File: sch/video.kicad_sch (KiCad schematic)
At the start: 16 parts

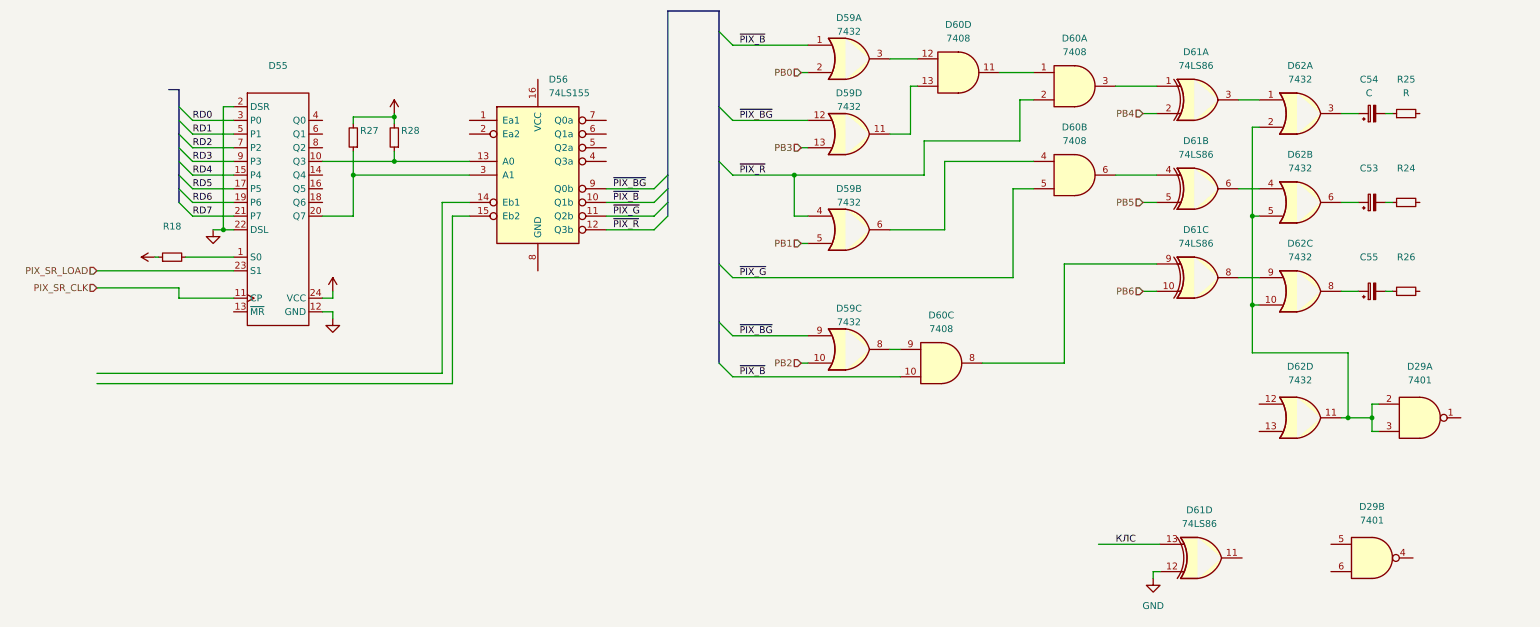
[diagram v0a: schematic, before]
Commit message: Video part schematic almost complete
No output connector added, also it needs some review / reality check.
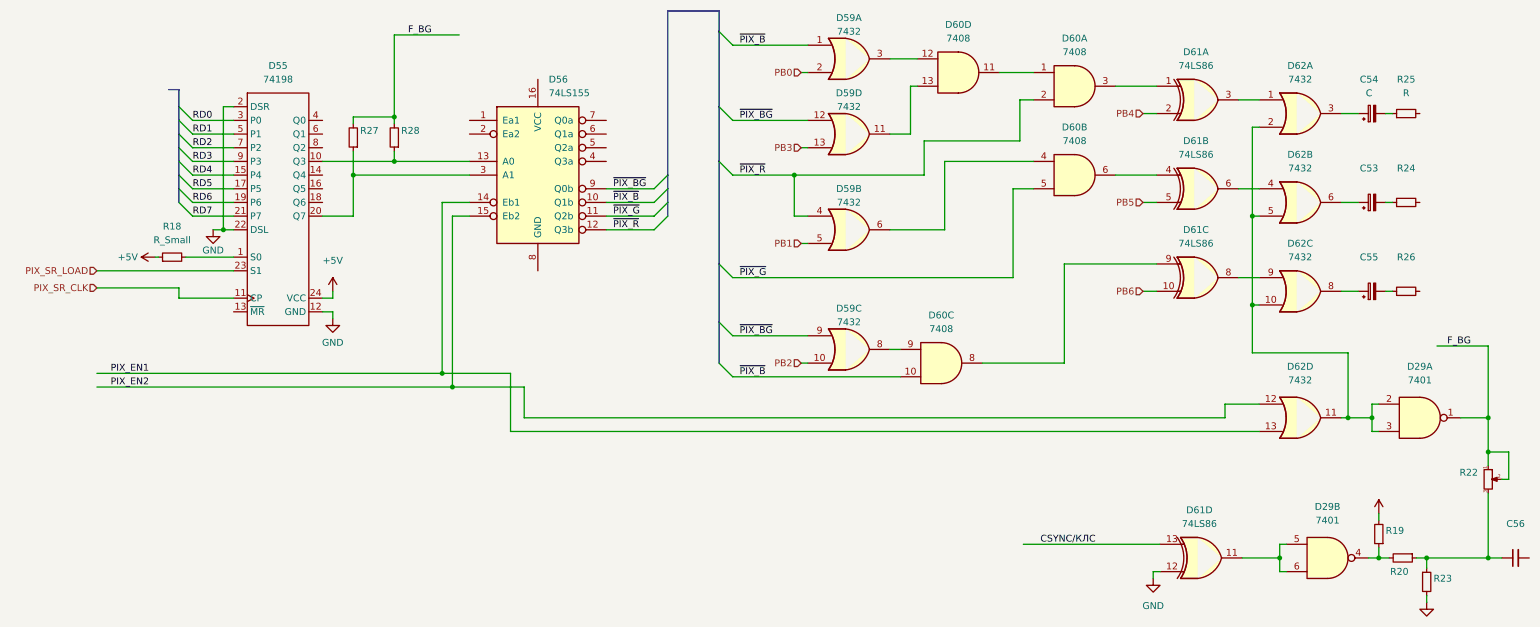
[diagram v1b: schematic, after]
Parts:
- added C56: (no value), symbol Device:C_Small
- added R19, R20, R23: ~, symbol Device:R_Small
- added R22: (no value), symbol Device:R_Potentiometer_Small
- D55: value (none) -> 74198
- R18: value (none) -> R_Small
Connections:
- net +5V: now also R19.2; no longer R27.2, R28.2
- net GND: now also R23.2
- net PIX_EN1: now reaches D56.14 (Eb1)
- net PIX_EN1: now also D62.13
- net PIX_EN2: now reaches D56.15 (Eb2)
- net PIX_EN2: now also D62.12
- net at D61.11: now also D29.5, D29.6
- net at D29.4: now also R19.1, R20.2
- net F_BG: now reaches D29.1
- net F_BG: now also R27.2, R28.2, R22.1, R22.2
- net КЛС renamed CSYNC/КЛС
- new net: C56.1, R20.1, R22.3, R23.1
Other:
- moved on the sheet: D29B

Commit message: Sch: added PIO sheet
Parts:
- C56: value (none) -> C_Small
- R22: value (none) -> !
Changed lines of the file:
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@@
       (effects (font (size 1.27 1.27)) hide)
     )
-    (property "Value" "" (id 1) (at 344.805 125.095 0))
+    (property "Value" "+5V" (id 1) (at 344.805 125.095 0))
     (property "Footprint" "" (id 2) (at 344.805 128.905 0)
       (effects (font (size 1.27 1.27)) hide)
@@
       (effects (font (size 1.27 1.27)) (justify right))
     )
-    (property "Value" "" (id 1) (at 363.22 123.8249 0)
+    (property "Value" "!" (id 1) (at 363.22 123.8249 0)
       (effects (font (size 1.27 1.27)) (justify right))
     )
@@
     (in_bom yes) (on_board yes) (fields_autoplaced)
     (property "Reference" "C56" (id 0) (at 370.2113 130.81 90))
-    (property "Value" "" (id 1) (at 370.2113 133.35 90))
+    (property "Value" "C_Small" (id 1) (at 370.2113 133.35 90))
     (property "Footprint" "" (id 2) (at 370.205 137.16 0)
       (effects (font (size 1.27 1.27)) hide)
@@
       (effects (font (size 1.27 1.27)) hide)
     )
-    (property "Value" "" (id 1) (at 353.695 149.86 0))
+    (property "Value" "GND" (id 1) (at 353.695 149.86 0))
     (property "Footprint" "" (id 2) (at 353.695 145.415 0)
       (effects (font (size 1.27 1.27)) hide)

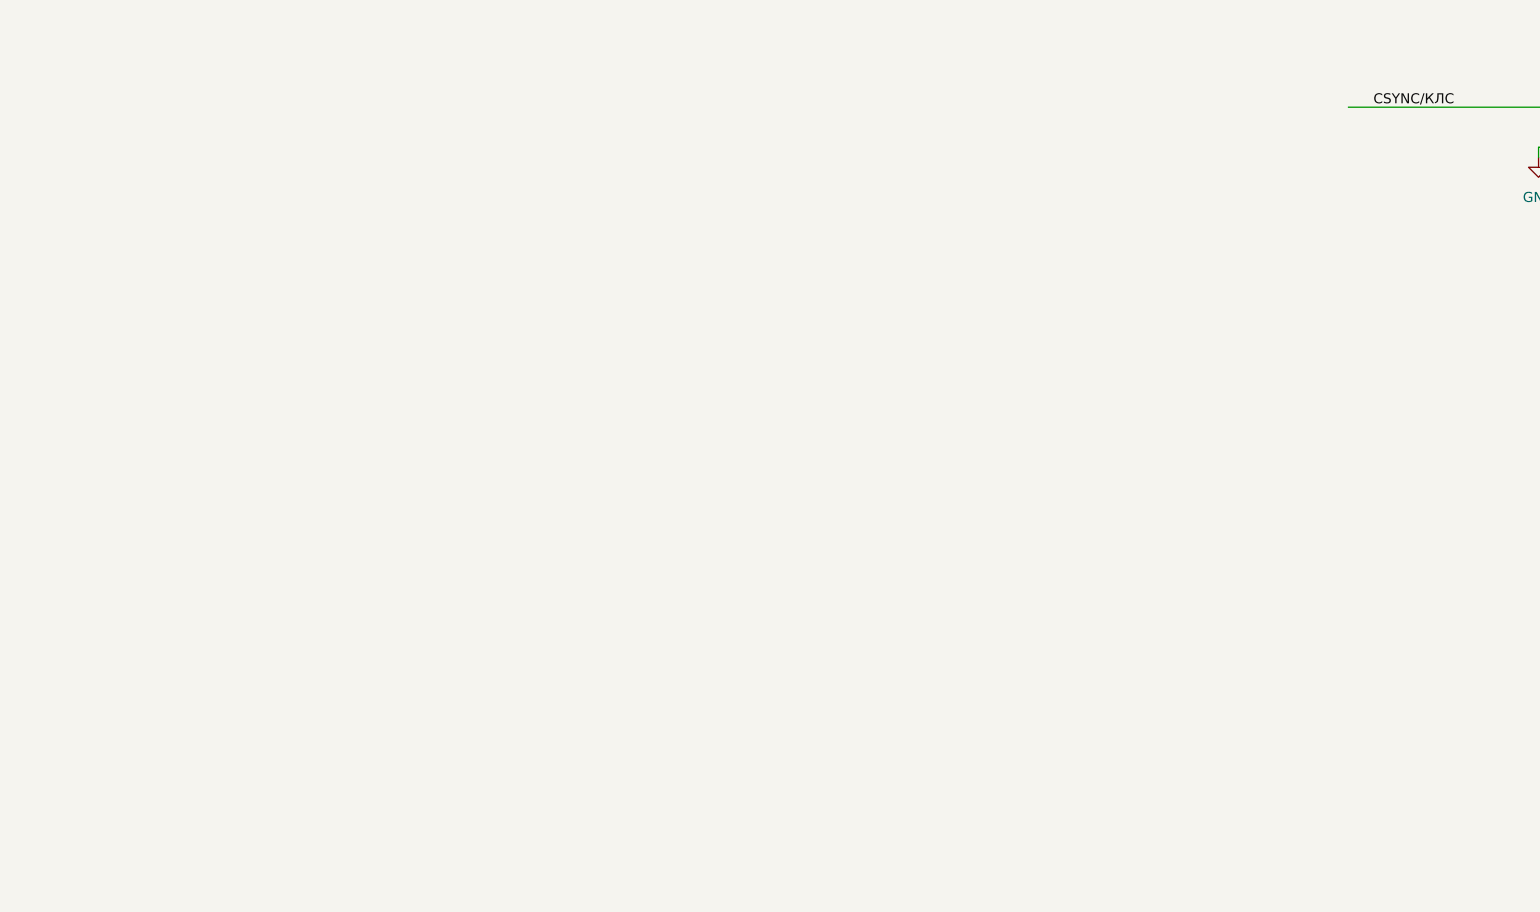
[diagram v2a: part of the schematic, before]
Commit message: Sch: timing counters block completed
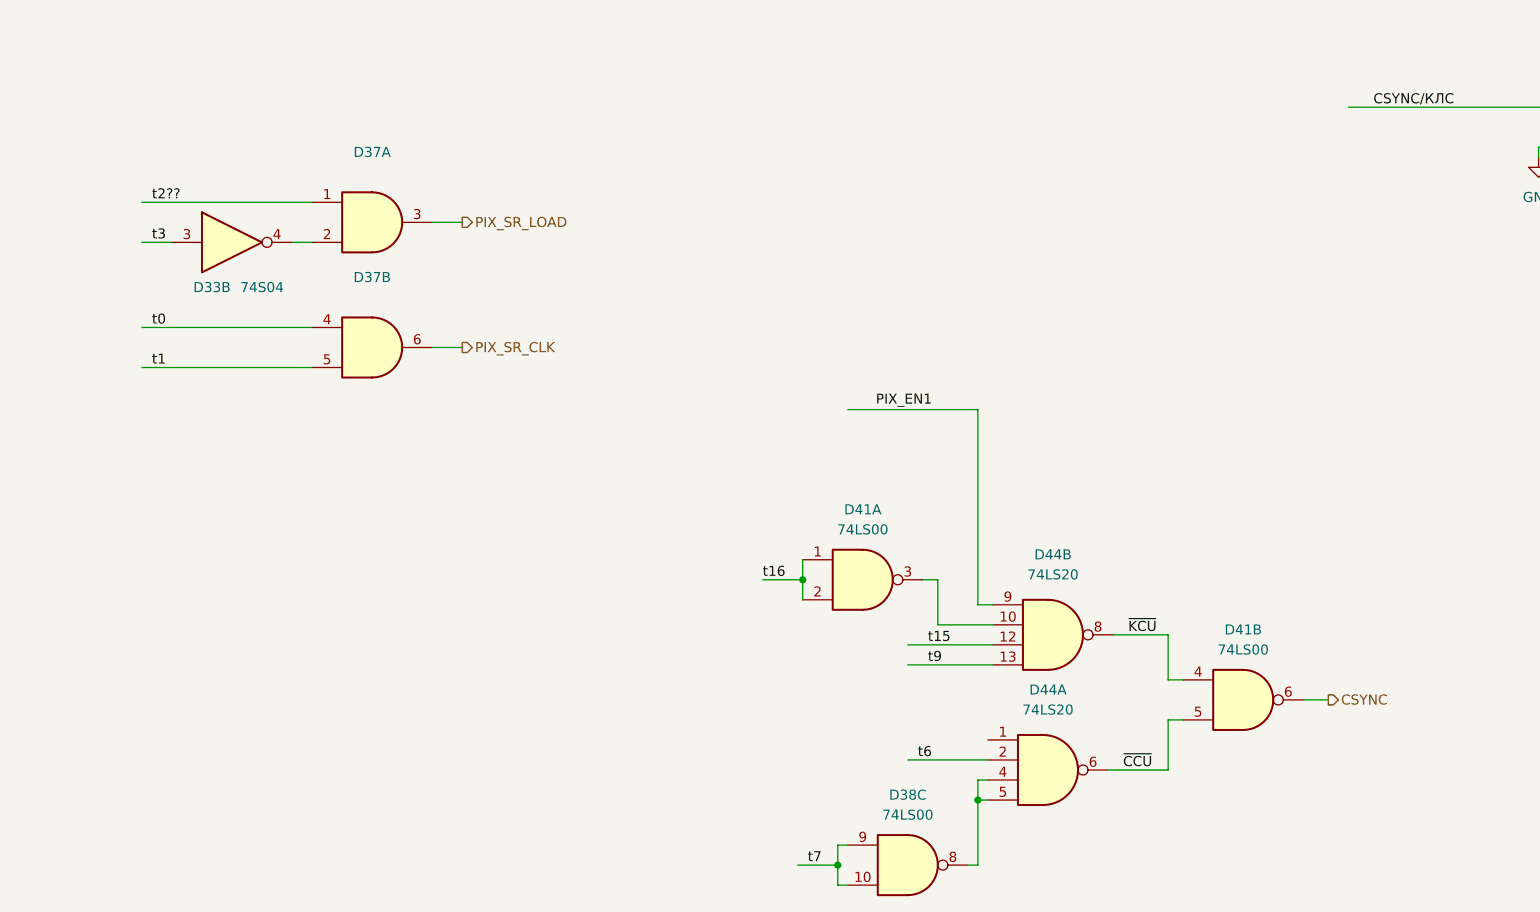
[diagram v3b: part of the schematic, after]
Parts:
- added D33: 74S04, symbol 74xx:74LS04
- added D37: ~, symbol 74xx:74LS08
- added D38, D41: 74LS00, symbol 74xx:74LS00
- added D44: 74LS20, symbol 74xx:74LS20
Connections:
- net PIX_SR_CLK: now also D37.6
- net PIX_SR_LOAD: now also D37.3
- new net: D41.3, D44.10
- new net: D33.4, D37.2
- new net: D38.8, D44.4, D44.5
- new net CSYNC: D41.6
- new net t0: D37.4
- new net t1: D37.5
- new net t15: D44.12
- new net t16: D41.1, D41.2
- new net t2??: D37.1
- new net t3: D33.3
- new net t6: D44.2
- new net t7: D38.10, D38.9
- new net t9: D44.13
- new net ~{CCU}: D41.5, D44.6
- new net ~{KCU}: D41.4, D44.8

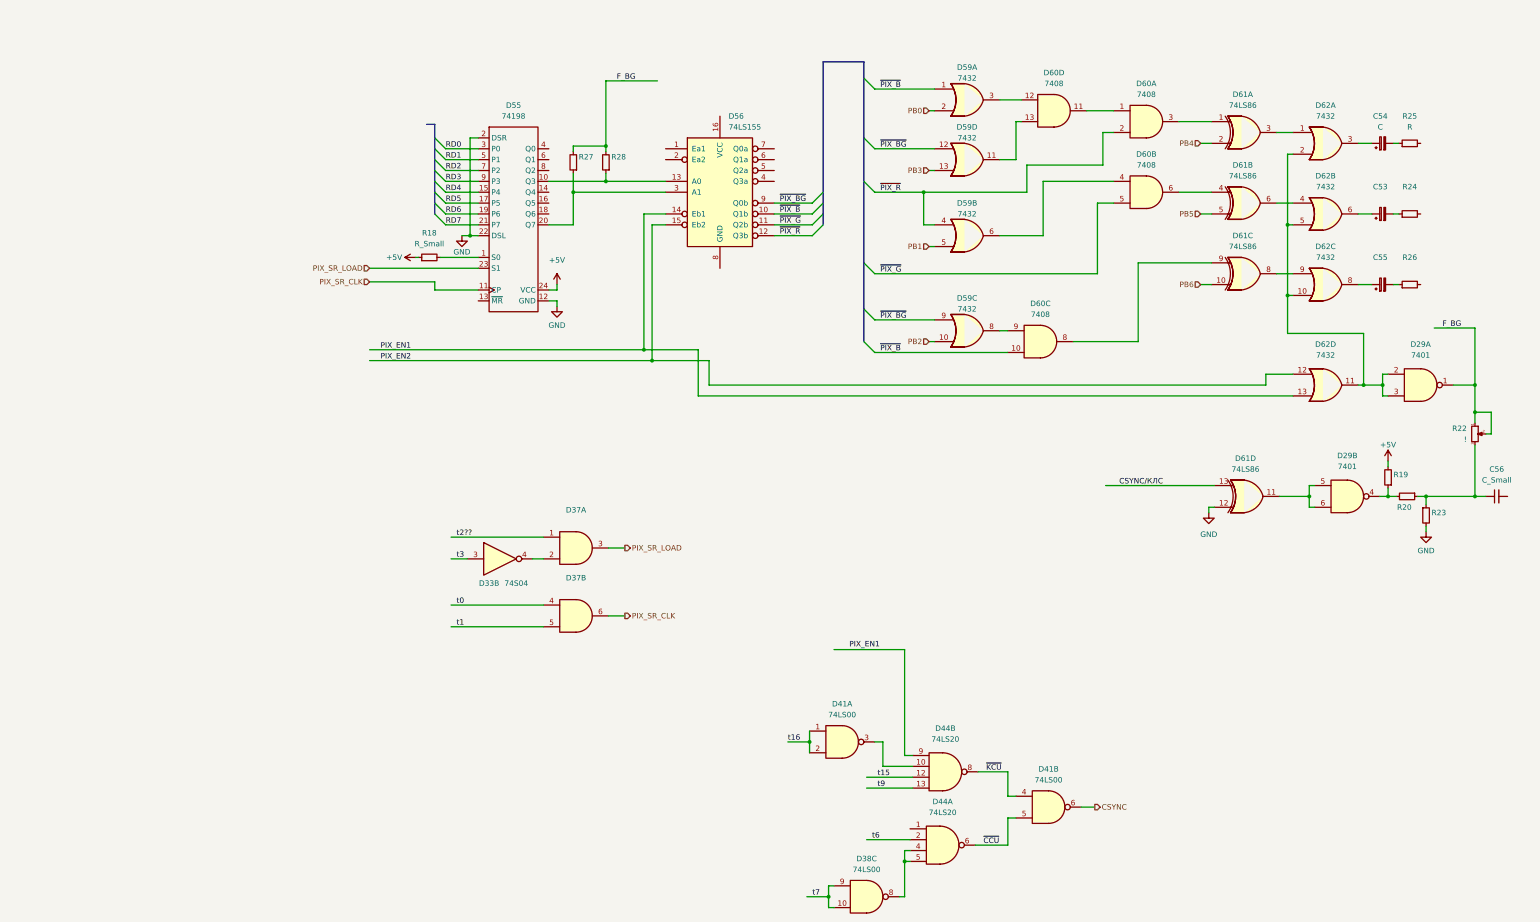
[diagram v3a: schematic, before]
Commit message: Sch: video block rework
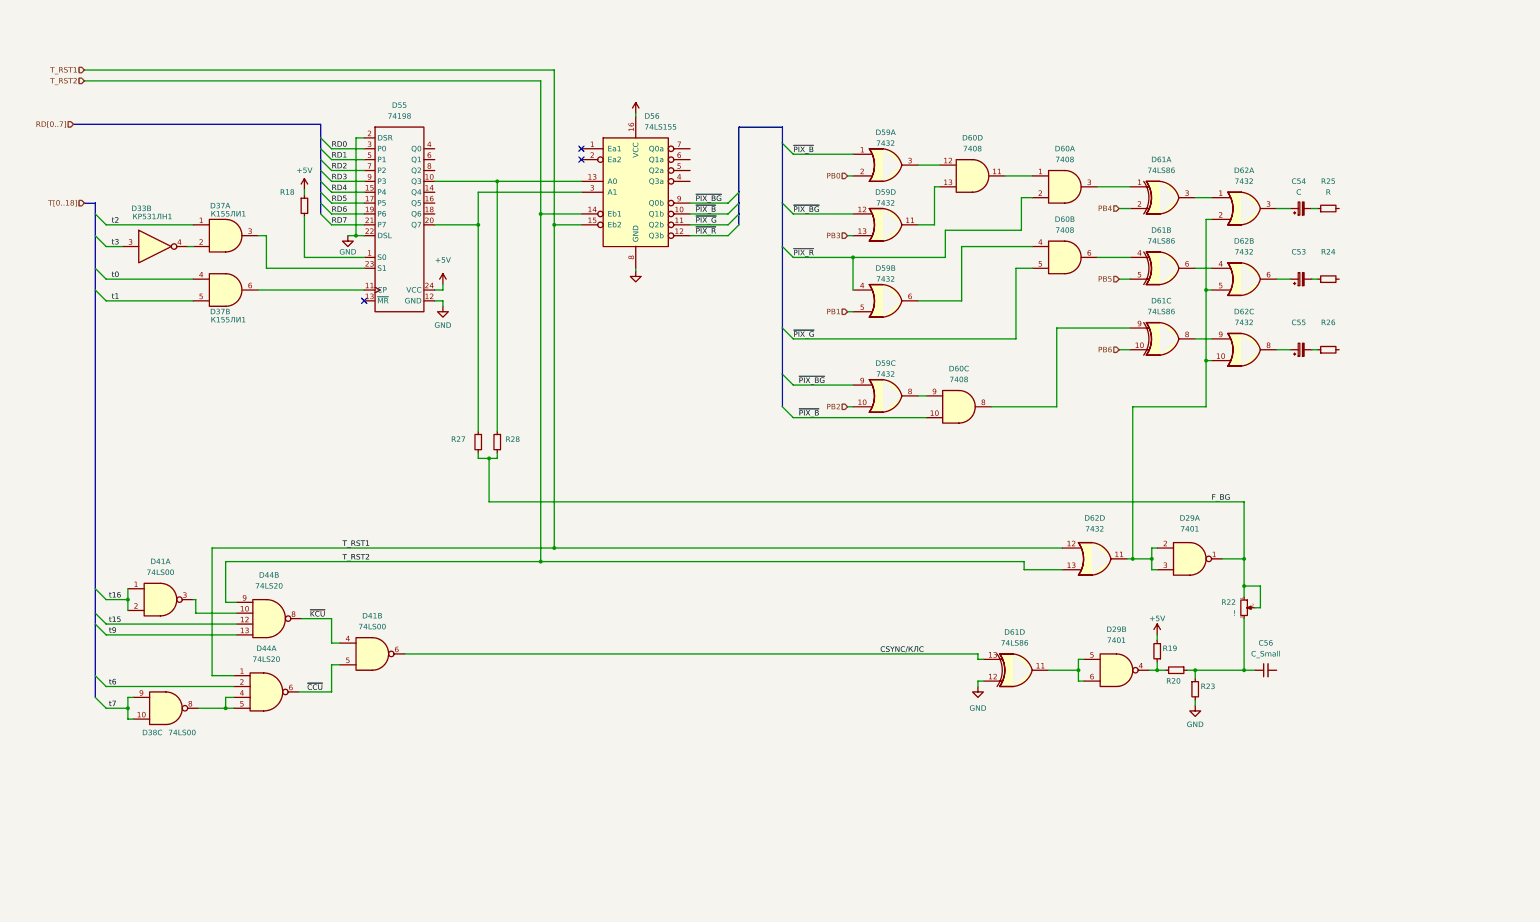
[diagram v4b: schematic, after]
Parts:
- D33: value 74S04 -> (none); CCCP (none) -> КР531ЛН1
- D37: value ~ -> (none); CCCP (none) -> К155ЛИ1
- R18: value R_Small -> (none)
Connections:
- net CSYNC is gone; now on net CSYNC/КЛС: D41.6
- net PIX_EN1 is gone; now on net T_RST2: D56.14 (Eb1), D62.13
- net PIX_EN2 is gone; now on net T_RST1: D56.15 (Eb2), D62.12
- net +5V: now also D56.16 (VCC)
- net GND: now also D56.8 (GND)
- net T_RST2: now reaches D44.9
- net T_RST1: now reaches D44.1
- net PIX_SR_CLK: no longer names the net of D37.6, D55.11 (CP)
- net PIX_SR_LOAD: no longer names the net of D37.3, D55.23 (S1)
- net t2?? renamed t2
- no-connect marks 0 -> 3
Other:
- moved on the sheet: C53, C54, C55, C56, D29A, D29B, D33B, D37A, D37B, D38C, D41A, D41B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

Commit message: Sch: video block cleanup in progress
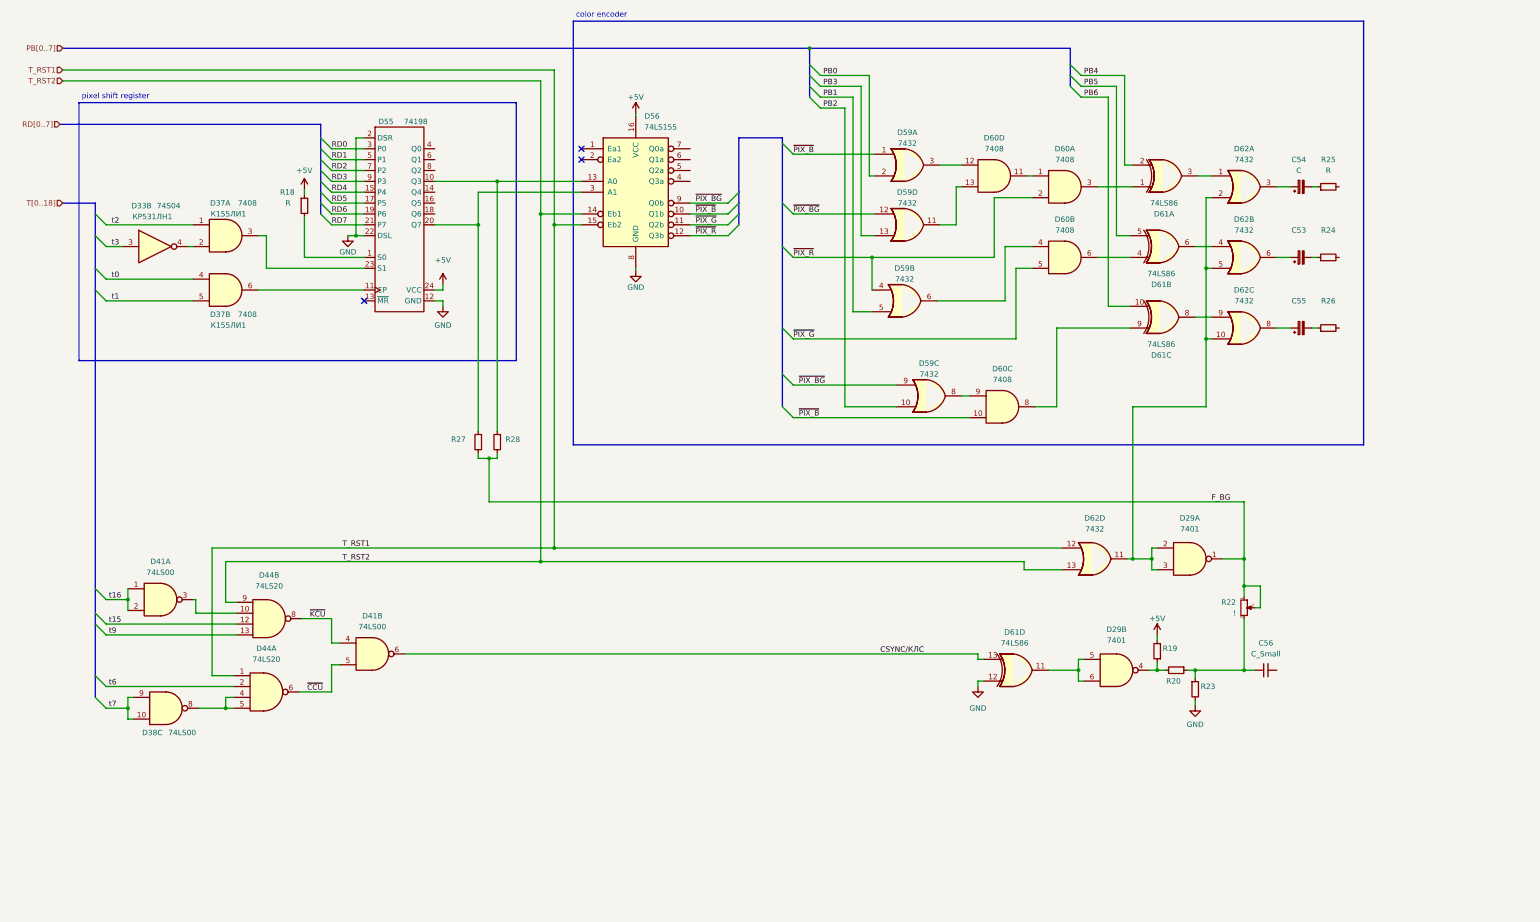
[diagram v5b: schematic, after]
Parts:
- D33: value (none) -> 74S04
- D37: value (none) -> 7408
- R18: value (none) -> R
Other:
- note added: "color encoder"
- note added: "pixel shift register"
- moved on the sheet: C53, C54, C55, D59A, D59B, D59C, D59D, D60C, D60D, D61A, D61B, D61C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
